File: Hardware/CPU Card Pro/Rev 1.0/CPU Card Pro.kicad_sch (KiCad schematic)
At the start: 18 parts, among them J1 6502 Card Edge, J2 BANK ADDR, J3 EXP, U1 65C816, U2 74HC00, U3 74HC245, U4 74HC573, X1 OCXO-14

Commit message: Fix title on CPU Card Pro sheets
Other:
- title: 6502 CPU Card -> 6502 CPU Card Pro
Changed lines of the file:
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@@
 	(paper "USLetter")
 	(title_block
-		(title "6502 CPU Card")
+		(title "6502 CPU Card Pro")
 		(date "2025-10-19")
 		(rev "1.0")

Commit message: RAM Card PCB
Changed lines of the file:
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@@
 	)
 	(global_label "BA4"
-		(shape bidirectional)
+		(shape output)
 		(at 133.35 120.65 0)
 		(effects
@@
 	)
 	(global_label "BA1"
-		(shape bidirectional)
+		(shape output)
 		(at 133.35 113.03 0)
 		(effects
@@
 	)
 	(global_label "BA7"
-		(shape bidirectional)
+		(shape input)
 		(at 177.8 121.92 0)
 		(effects
@@
 	)
 	(global_label "BA0"
-		(shape bidirectional)
+		(shape input)
 		(at 158.75 114.3 180)
 		(effects
@@
 	)
 	(global_label "BA2"
-		(shape bidirectional)
+		(shape input)
 		(at 158.75 116.84 180)
 		(effects
@@
 	)
 	(global_label "BA5"
-		(shape bidirectional)
+		(shape output)
 		(at 133.35 123.19 0)
 		(effects
@@
 	)
 	(global_label "BA2"
-		(shape bidirectional)
+		(shape output)
 		(at 133.35 115.57 0)
 		(effects
@@
 	)
 	(global_label "BA6"
-		(shape bidirectional)
+		(shape input)
 		(at 158.75 121.92 180)
 		(effects
@@
 	)
 	(global_label "BA5"
-		(shape bidirectional)
+		(shape input)
 		(at 177.8 119.38 0)
 		(effects
@@
 	)
 	(global_label "BA3"
-		(shape bidirectional)
+		(shape output)
 		(at 133.35 118.11 0)
 		(effects
@@
 	)
 	(global_label "BA7"
-		(shape bidirectional)
+		(shape output)
 		(at 133.35 128.27 0)
 		(effects
@@
 	)
 	(global_label "BA3"
-		(shape bidirectional)
+		(shape input)
 		(at 177.8 116.84 0)
 		(effects
@@
 	)
 	(global_label "BA6"
-		(shape bidirectional)
+		(shape output)
 		(at 133.35 125.73 0)
 		(effects
@@
 	)
 	(global_label "BA0"
-		(shape bidirectional)
+		(shape output)
 		(at 133.35 110.49 0)
 		(effects
@@
 	)
 	(global_label "BA4"
-		(shape bidirectional)
+		(shape input)
 		(at 158.75 119.38 180)
 		(effects
@@
 	)
 	(global_label "BA1"
-		(shape bidirectional)
+		(shape input)
 		(at 177.8 114.3 0)
 		(effects

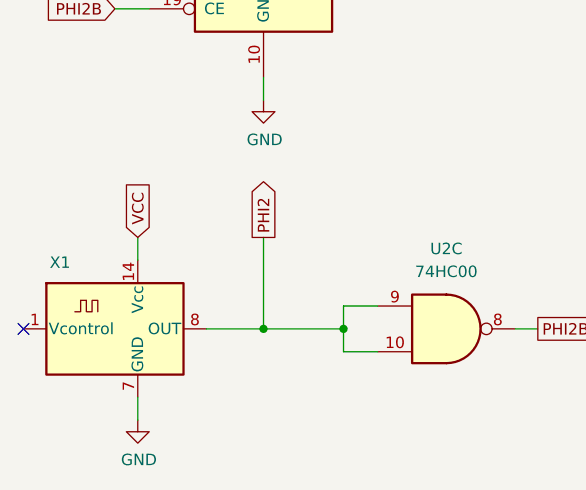
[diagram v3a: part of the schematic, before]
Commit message: Remove oscillator from CPU cards
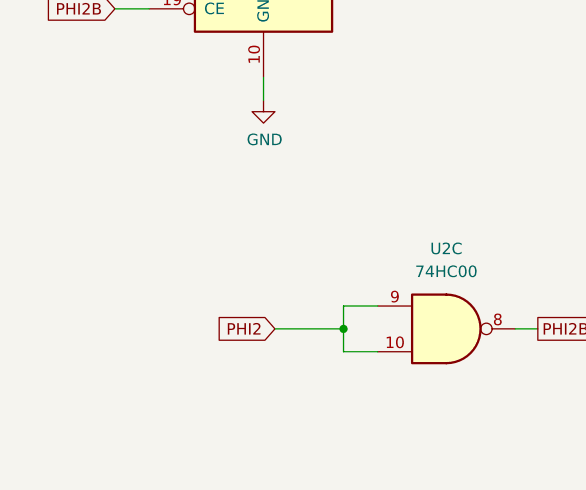
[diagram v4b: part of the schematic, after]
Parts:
- removed X1: OCXO-14, Oscillator:Oscillator_DIP-14, symbol Oscillator:OCXO-14
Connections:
- no-connect marks 2 -> 1
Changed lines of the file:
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@@
 	)
 	(junction
-		(at 50.8 171.45)
-		(diameter 0)
-		(color 0 0 0 0)
-	)
-	(junction
 		(at 229.87 119.38)
 		(diameter 0)
@@
 		(at 237.49 149.86)
 	)
-	(no_connect
-		(at 24.13 171.45)
-	)
 	(wire
 		(pts
@@
 	(wire
 		(pts
-			(xy 36.83 161.29) (xy 36.83 163.83)
-		)
-		(stroke
-			(width 0)
-			(type default)
-		)
-	)
-	(wire
-		(pts
 			(xy 97.79 45.72) (xy 100.33 45.72)
 		)
@@
 	(wire
 		(pts
-			(xy 36.83 179.07) (xy 36.83 181.61)
-		)
-		(stroke
-			(width 0)
-			(type default)
-		)
-	)
-	(wire
-		(pts
 			(xy 33.02 55.88) (xy 35.56 55.88)
 		)
@@
 	(wire
 		(pts
-			(xy 50.8 171.45) (xy 59.69 171.45)
-		)
-		(stroke
-			(width 0)
-			(type default)
-		)
-	)
-	(wire
-		(pts
 			(xy 91.44 128.27) (xy 102.87 128.27)
 		)
@@
 	(wire
 		(pts
-			(xy 44.45 171.45) (xy 50.8 171.45)
-		)
-		(stroke
-			(width 0)
-			(type default)
-		)
-	)
-	(wire
-		(pts
 			(xy 198.12 92.71) (xy 198.12 96.52)
 		)
@@
 	(wire
 		(pts
-			(xy 50.8 161.29) (xy 50.8 171.45)
+			(xy 52.07 171.45) (xy 59.69 171.45)
 		)
 		(stroke
@@
 		)
 	)
-	(global_label "VCC"
-		(shape input)
-		(at 36.83 161.29 90)
-		(fields_autoplaced yes)
-		(effects
-			(font
-				(size 1.27 1.27)
-			)
-			(justify left)
-		)
-		(property "Intersheetrefs" "${INTERSHEET_REFS}"
-			(at 36.83 155.3304 90)
-			(effects
-				(font
-					(size 1.27 1.27)
-				)
-				(justify left)
-				(hide yes)
-			)
-		)
-	)
 	(global_label "ABORTB"
 		(shape input)
@@
 	)
 	(global_label "PHI2"
-		(shape output)
-		(at 50.8 161.29 90)
+		(shape input)
+		(at 52.07 171.45 180)
 		(fields_autoplaced yes)
 		(effects
@@
 				(size 1.27 1.27)
 			)
-			(justify left)
+			(justify right)
 		)
 		(property "Intersheetrefs" "${INTERSHEET_REFS}"
-			(at 50.8 154.5442 90)
+			(at 45.3242 171.45 0)
 			(effects
 				(font
 					(size 1.27 1.27)
 				)
-				(justify left)
+				(justify right)
 				(hide yes)
 			)
@@
 	)
 	(symbol
-		(lib_id "Oscillator:OCXO-14")
-		(at 36.83 171.45 0)
-		(unit 1)
-		(exclude_from_sim no)
-		(in_bom no)
-		(on_board yes)
-		(dnp no)
-		(property "Reference" "X1"
-			(at 28.194 164.084 0)
-			(effects
-				(font
-					(size 1.27 1.27)
-				)
-			)
-		)
-		(property "Value" "OCXO-14"
-			(at 48.26 167.6714 0)
-			(effects
-				(font
-					(size 1.27 1.27)
-				)
-				(hide yes)
-			)
-		)
-		(property "Footprint" "Oscillator:Oscillator_DIP-14"
-			(at 48.26 180.34 0)
-			(effects
-				(font
-					(size 1.27 1.27)
-				)
-				(hide yes)
-			)
-		)
-		(property "Datasheet" "http://www.petermann-technik.de/fileadmin/petermann/pdf/crystal-oscillators/OCXO-14_PETERMANN-TECHNIK.pdf"
-			(at 29.21 168.91 0)
-			(effects
-				(font
-					(size 1.27 1.27)
-				)
-				(hide yes)
-			)
-		)
-		(property "Description" "Voltage-Controlled Crystal Clock Oscillator, DIP14-style metal package"
-			(at 36.83 171.45 0)
-			(effects
-				(font
-					(size 1.27 1.27)
-				)
-				(hide yes)
-			)
-		)
-		(pin "14"
-		)
-		(pin "1"
-		)
-		(pin "7"
-		)
-		(pin "8"
-		)
-		(instances
-			(project "CPU Card"
-				(path "/b93a1794-fe4c-46dd-b3af-a8a2c2dc45ce"
-					(reference "X1")
-					(unit 1)
-				)
-			)
-		)
-	)
-	(symbol
 		(lib_id "power:GND")
 		(at 177.8 127 0)
@@
 					(unit 1)
 				)
-			)
-		)
-	)
-	(symbol
-		(lib_id "power:GND")
-		(at 36.83 181.61 0)
-		(unit 1)
-		(exclude_from_sim no)
-		(in_bom yes)
-		(on_board yes)
-		(dnp no)
-		(property "Reference" "#PWR08"
-			(at 36.83 187.96 0)
-			(effects
-				(font
-					(size 1.27 1.27)
-				)
-				(hide yes)
-			)
-		)
-		(property "Value" "GND"
-			(at 36.957 186.0042 0)
-			(effects
-				(font
-					(size 1.27 1.27)
-				)
-			)
-		)
-		(property "Footprint" ""
-			(at 36.83 181.61 0)
-			(effects
-				(font
-					(size 1.27 1.27)
-				)
-				(hide yes)
-			)
-		)
-		(property "Datasheet" ""
-			(at 36.83 181.61 0)
-			(effects
-				(font
-					(size 1.27 1.27)
-				)
-				(hide yes)
-			)
-		)
-		(property "Description" "Power symbol creates a global label with name \"GND\" , ground"
-			(at 36.83 181.61 0)
-			(effects
-				(font
-					(size 1.27 1.27)
-				)
-				(hide yes)
-			)
-		)
-		(pin "1"
-		)
-		(instances
-			(project "CPU Card"
-				(path "/b93a1794-fe4c-46dd-b3af-a8a2c2dc45ce"
-					(reference "#PWR08")
-					(unit 1)
-				)
